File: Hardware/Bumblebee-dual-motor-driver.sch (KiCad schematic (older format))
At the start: 54 parts

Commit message: Assigned all footprints.
Still need to pick and check FET footprint, pick pot.
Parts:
- C10, C3, C4, C5, C6, C7, C8, C9: renamed from C?; footprint (none) -> Capacitor_SMD:C_0603_1608Metric
- D1, D2: renamed from D?; footprint (none) -> LED_SMD:LED_0603_1608Metric
- F1, F2: renamed from F?; footprint (none) -> Fuse:Fuseholder_Blade_Mini_Keystone_3568
- J10, J11, J12, J13, J14, J15, J16, J7, J8, J9: renamed from J?; footprint (none) -> TE_1217861-1:TE_1217861-1
- J2: renamed from J?; footprint (none) -> Connector_USB:USB_Micro-B_Molex-105017-0001
- J3: renamed from J?; footprint (none) -> Connector_PinSocket_2.54mm:PinSocket_1x04_P2.54mm_Vertical
- J4: renamed from J?; footprint (none) -> Connector_PinSocket_2.54mm:PinSocket_1x08_P2.54mm_Vertical
- J5: renamed from J?; footprint (none) -> Connector_JST:JST_XH_B4B-XH-A_1x04_P2.50mm_Vertical
- J6: renamed from J?; footprint (none) -> Connector_JST:JST_XH_B8B-XH-A_1x08_P2.50mm_Vertical
- R1, R2: renamed from R?; footprint (none) -> Resistor_SMD:R_0603_1608Metric
- U1: renamed from U?; symbol interface-board-rescue:ATmega328P-AU-MCU_Microchip_ATmega -> Bumblebee-dual-motor-driver-rescue:ATmega328P-AU-MCU_Microchip_ATmega-interface-board-rescue
- gave numbers to parts that had none: 19

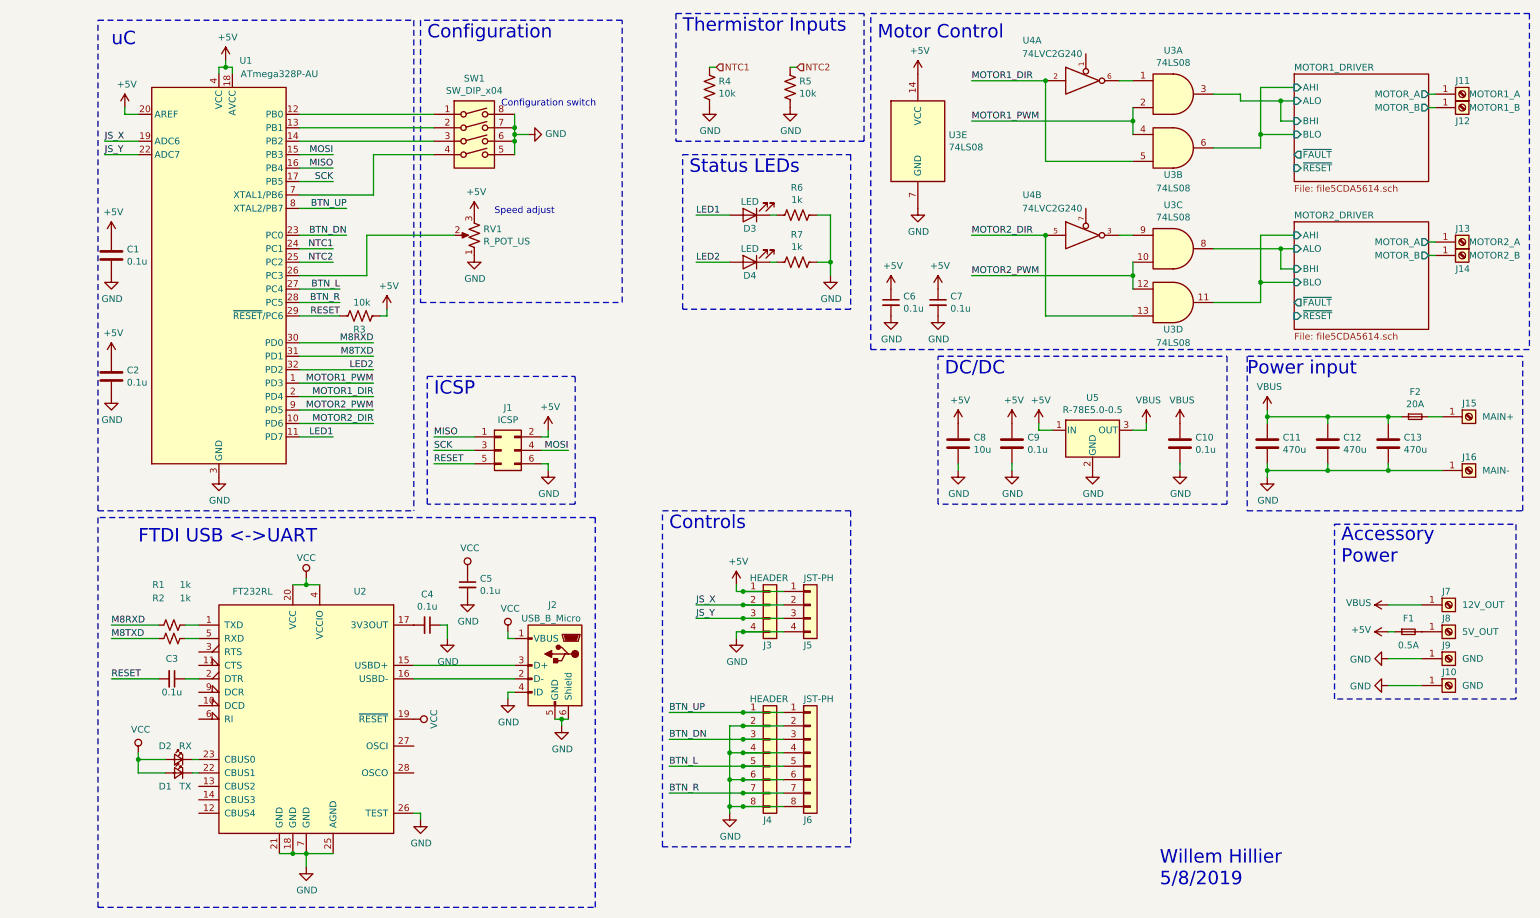
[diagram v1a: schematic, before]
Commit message: Started moving components around on PCB.
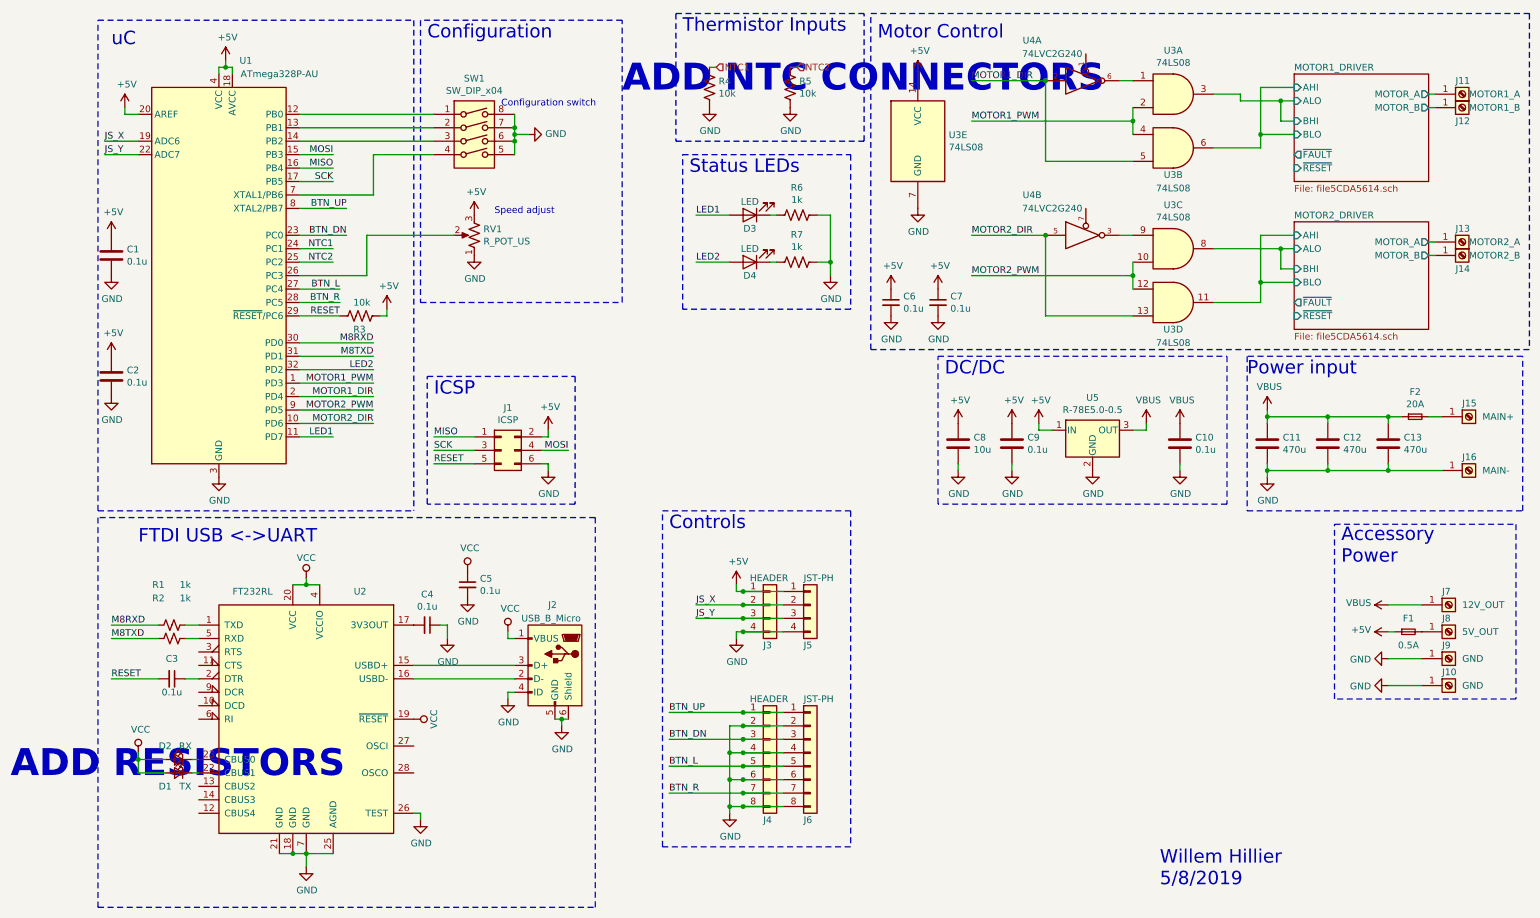
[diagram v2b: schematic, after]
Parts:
- C11, C12, C13: footprint (none) -> Capacitor_SMD:C_Elec_10x10.2
- RV1: footprint (none) -> Potentiometer_SMD:Potentiometer_ACP_CA6-VSMD_Vertical
- SW1: footprint (none) -> Button_Switch_SMD:SW_DIP_SPSTx04_Slide_6.7x11.72mm_W6.73mm_P2.54mm_LowProfile_JPin
- U3: footprint (none) -> Package_SO:SOIC-14_3.9x8.7mm_P1.27mm
- U4: footprint (none) -> Package_SO:TSSOP-8_3x3mm_P0.65mm
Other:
- note added: "ADD NTC CONNECTORS"
- note added: "ADD RESISTORS"
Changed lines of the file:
@@
 F 0 "U4" H 7500 1300 50  0000 C CNN
 F 1 "74LVC2G240" H 7650 1200 50  0000 C CNN
-F 2 "" H 7900 1000 50  0001 C CNN
+F 2 "Package_SO:TSSOP-8_3x3mm_P0.65mm" H 7900 1000 50  0001 C CNN
 F 3 "http://www.ti.com/lit/sg/scyt129e/scyt129e.pdf" H 7900 1000 50  0001 C CNN
 	1    7900 1000
@@
 F 0 "U4" H 7500 2450 50  0000 C CNN
 F 1 "74LVC2G240" H 7650 2350 50  0000 C CNN
-F 2 "" H 7900 2150 50  0001 C CNN
+F 2 "Package_SO:TSSOP-8_3x3mm_P0.65mm" H 7900 2150 50  0001 C CNN
 F 3 "http://www.ti.com/lit/sg/scyt129e/scyt129e.pdf" H 7900 2150 50  0001 C CNN
 	2    7900 2150
@@
 F 0 "U3" H 8550 1425 50  0000 C CNN
 F 1 "74LS08" H 8550 1334 50  0000 C CNN
-F 2 "" H 8550 1100 50  0001 C CNN
+F 2 "Package_SO:SOIC-14_3.9x8.7mm_P1.27mm" H 8550 1100 50  0001 C CNN
 F 3 "http://www.ti.com/lit/gpn/sn74LS08" H 8550 1100 50  0001 C CNN
 	1    8550 1100
@@
 F 0 "U3" H 8550 1300 50  0000 C CNN
 F 1 "74LS08" H 8550 1200 50  0000 C CNN
-F 2 "" H 8550 1500 50  0001 C CNN
+F 2 "Package_SO:SOIC-14_3.9x8.7mm_P1.27mm" H 8550 1500 50  0001 C CNN
 F 3 "http://www.ti.com/lit/gpn/sn74LS08" H 8550 1500 50  0001 C CNN
 	2    8550 1500
@@
 F 0 "U3" H 8550 2575 50  0000 C CNN
 F 1 "74LS08" H 8550 2484 50  0000 C CNN
-F 2 "" H 8550 2250 50  0001 C CNN
+F 2 "Package_SO:SOIC-14_3.9x8.7mm_P1.27mm" H 8550 2250 50  0001 C CNN
 F 3 "http://www.ti.com/lit/gpn/sn74LS08" H 8550 2250 50  0001 C CNN
 	3    8550 2250
@@
 F 0 "U3" H 8550 2450 50  0000 C CNN
 F 1 "74LS08" H 8550 2350 50  0000 C CNN
-F 2 "" H 8550 2650 50  0001 C CNN
+F 2 "Package_SO:SOIC-14_3.9x8.7mm_P1.27mm" H 8550 2650 50  0001 C CNN
 F 3 "http://www.ti.com/lit/gpn/sn74LS08" H 8550 2650 50  0001 C CNN
 	4    8550 2650
@@
 F 0 "U3" H 6880 1496 50  0000 L CNN
 F 1 "74LS08" H 6880 1405 50  0000 L CNN
-F 2 "" H 6650 1450 50  0001 C CNN
+F 2 "Package_SO:SOIC-14_3.9x8.7mm_P1.27mm" H 6650 1450 50  0001 C CNN
 F 3 "http://www.ti.com/lit/gpn/sn74LS08" H 6650 1450 50  0001 C CNN
 	5    6650 1450
@@
 F 0 "SW1" H 3350 1917 50  0000 C CNN
 F 1 "SW_DIP_x04" H 3350 1826 50  0000 C CNN
-F 2 "" H 3350 1450 50  0001 C CNN
+F 2 "Button_Switch_SMD:SW_DIP_SPSTx04_Slide_6.7x11.72mm_W6.73mm_P2.54mm_LowProfile_JPin" H 3350 1450 50  0001 C CNN
 F 3 "~" H 3350 1450 50  0001 C CNN
 	1    3350 1450
@@
 F 0 "RV1" H 3282 2104 50  0000 R CNN
 F 1 "R_POT_US" H 3282 2195 50  0000 R CNN
-F 2 "" H 3350 2150 50  0001 C CNN
+F 2 "Potentiometer_SMD:Potentiometer_ACP_CA6-VSMD_Vertical" H 3350 2150 50  0001 C CNN
 F 3 "~" H 3350 2150 50  0001 C CNN
 	1    3350 2150
@@
 F 0 "C13" H 10265 3746 50  0000 L CNN
 F 1 "470u" H 10265 3655 50  0000 L CNN
-F 2 "" H 10188 3550 50  0001 C CNN
+F 2 "Capacitor_SMD:C_Elec_10x10.2" H 10188 3550 50  0001 C CNN
 F 3 "~" H 10150 3700 50  0001 C CNN
 	1    10150 3700
@@
 F 0 "C12" H 9815 3746 50  0000 L CNN
 F 1 "470u" H 9815 3655 50  0000 L CNN
-F 2 "" H 9738 3550 50  0001 C CNN
+F 2 "Capacitor_SMD:C_Elec_10x10.2" H 9738 3550 50  0001 C CNN
 F 3 "~" H 9700 3700 50  0001 C CNN
 	1    9700 3700
@@
 F 0 "C11" H 9365 3746 50  0000 L CNN
 F 1 "470u" H 9365 3655 50  0000 L CNN
-F 2 "" H 9288 3550 50  0001 C CNN
+F 2 "Capacitor_SMD:C_Elec_10x10.2" H 9288 3550 50  0001 C CNN
 F 3 "~" H 9250 3700 50  0001 C CNN
 	1    9250 3700
@@
 Text Notes 3000 700  0    100  ~ 0
 Configuration
+Text Notes -100 6200 0    200  ~ 40
+ADD RESISTORS
+Text Notes 4450 1100 0    200  ~ 40
+ADD NTC CONNECTORS
 $EndSCHEMATC
